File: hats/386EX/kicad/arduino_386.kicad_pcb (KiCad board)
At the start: 2 copper layers, 102.9 x 57.1 mm, 19 parts, among them J1 Conn_01x02_Pin, U11 I386EX_PQFP

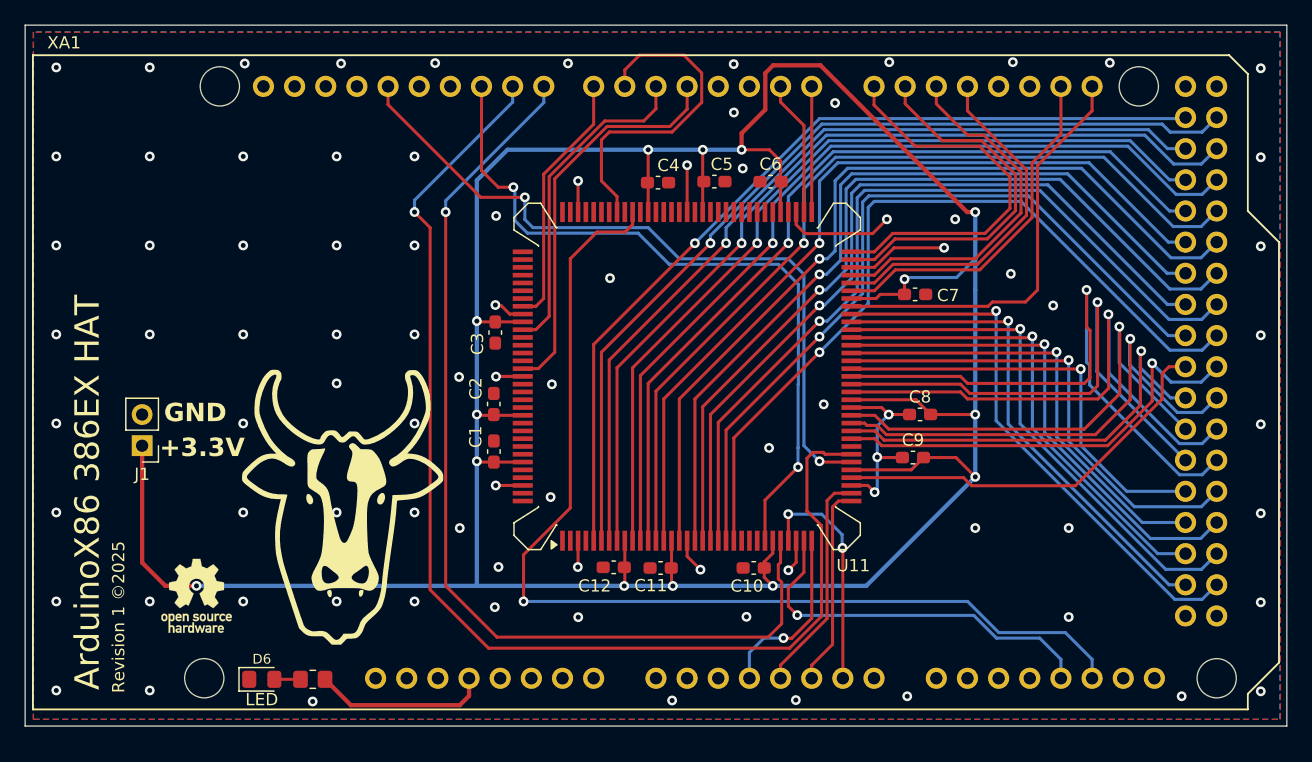
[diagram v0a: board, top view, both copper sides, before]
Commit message: add JTAG header, connect SMI pins
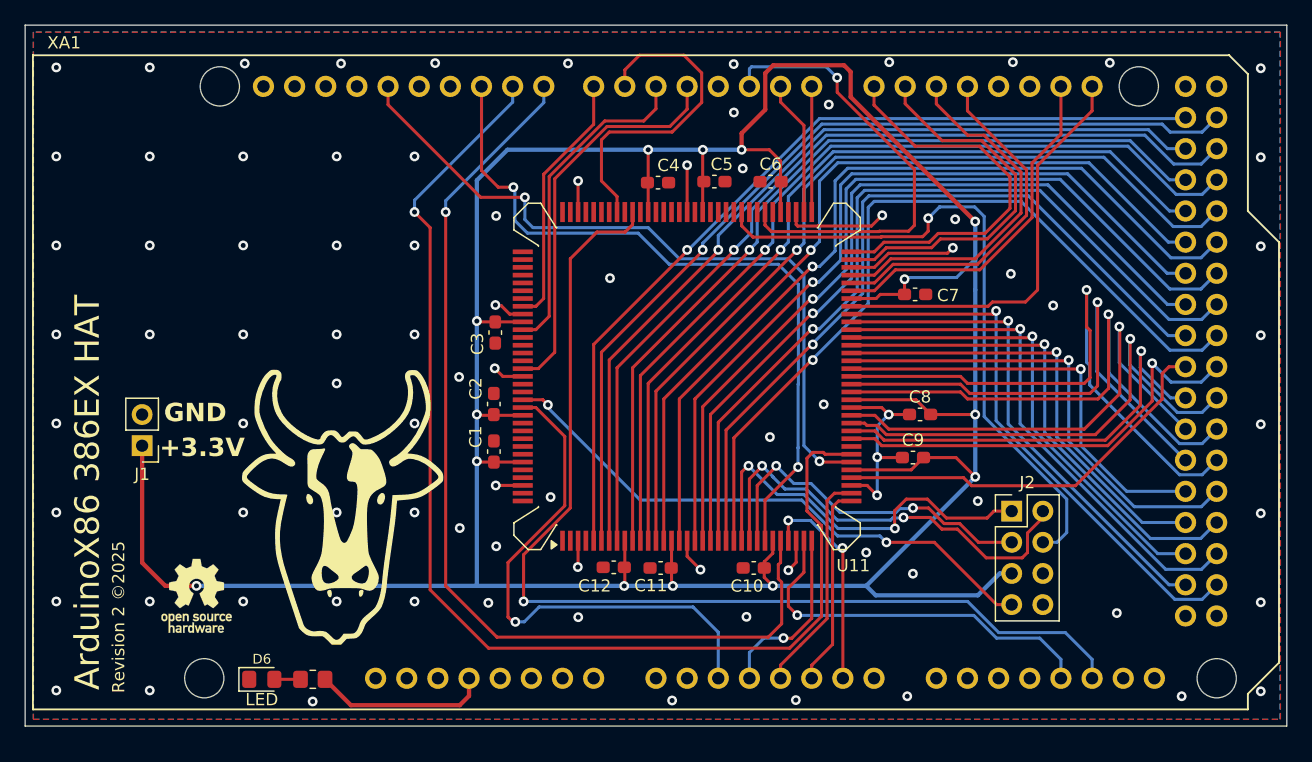
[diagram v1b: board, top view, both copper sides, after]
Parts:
- added J2: JTAG, Connector_PinHeader_2.54mm:PinHeader_2x04_P2.54mm_Vertical, F.Cu at (183.3, 106.9)
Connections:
- U11 pad 119: unconnected-(U11-TRST-Pad119) -> TRST
- U11 pad 120: unconnected-(U11-SMIACT-Pad120) -> SMIACT
- U11 pad 24: unconnected-(U11-TDO-Pad24) -> TDO
- U11 pad 25: unconnected-(U11-TDI-Pad25) -> TDI
- U11 pad 26: unconnected-(U11-TMS-Pad26) -> TMS
- U11 pad 73: unconnected-(U11-SMI-Pad73) -> SMI
- U11 pad 76: unconnected-(U11-TCK-Pad76) -> TCK
- XA1 pad A2: unconnected-(XA1-PadA2) -> SMIACT
- XA1 pad D2: /A24_A -> SMI
- XA1 pad D3: /A25_A -> unconnected-(XA1-D3_INT1-PadD3)
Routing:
- net TCK: track 0.00 -> 54.0 mm, vias 0 -> 1
- net TRST: track 0.00 -> 46.8 mm, vias 0 -> 2
- net SMIACT: track 0.00 -> 43.2 mm, vias 0 -> 1
- net SMI: track 0.00 -> 37.4 mm, vias 0 -> 1
- net TDI: track 0.00 -> 35.7 mm, vias 0 -> 2
- net TDO: track 0.00 -> 32.8 mm, vias 0 -> 2
- net TMS: track 0.00 -> 29.1 mm, vias 0 -> 2
- net +3.3VP: track 263.4 -> 277.1 mm
- net W/~{R}: track 19.2 -> 17.9 mm
- net GND: track 54.3 -> 55.1 mm
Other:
- board text added: "Revision 2 ©2025"
- board text removed: "Revision 1 ©2025"
